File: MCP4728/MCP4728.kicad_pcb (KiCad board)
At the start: 2 copper layers, 25.4 x 17.8 mm, 22 parts, among them J1 Conn_01x06, J2 Conn_01x04, J3 Conn_01x06, J4 Conn_01x04, U1 MCP4728

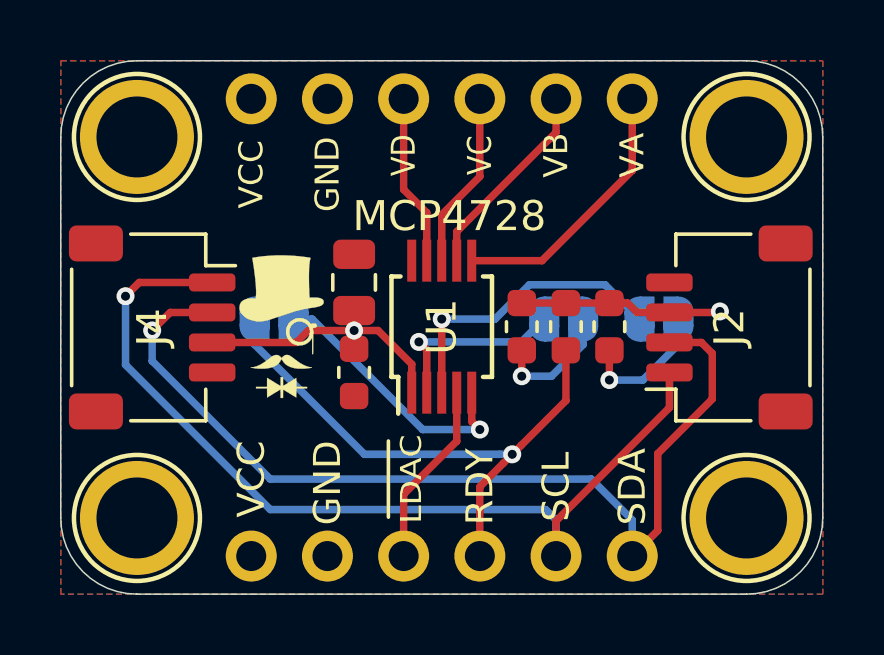
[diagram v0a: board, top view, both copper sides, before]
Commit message: Copper Pour Edits
Copper pour reduced to have 0.2mm edge clearance
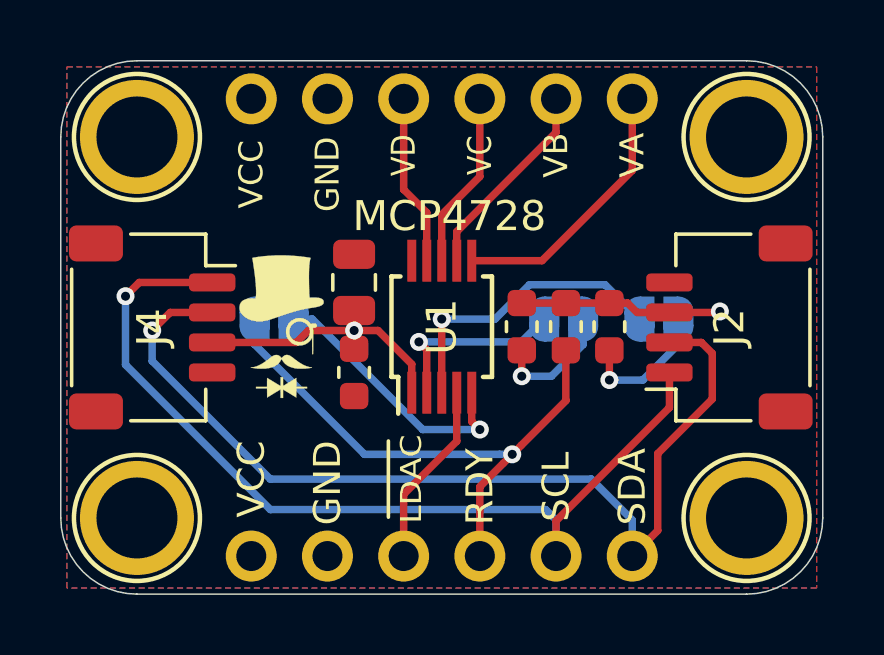
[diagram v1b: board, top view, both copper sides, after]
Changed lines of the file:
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@@
   )
   (setup
-    (last_trace_width 0.3)
+    (last_trace_width 0.127)
     (user_trace_width 0.2)
     (user_trace_width 0.25)
@@
     (polygon
       (pts
-        (xy 52.578 27.0764) (xy 77.978 27.0764) (xy 77.978 44.8564) (xy 52.578 44.8564)
+        (xy 52.7812 27.2796) (xy 77.7748 27.2796) (xy 77.7748 44.6532) (xy 52.7812 44.6532)
       )
     )
@@
     (polygon
       (pts
-        (xy 52.578 27.0764) (xy 77.978 27.0764) (xy 77.978 44.8564) (xy 52.578 44.8564)
+        (xy 52.7812 27.2796) (xy 77.7748 27.2796) (xy 77.7748 44.6532) (xy 52.7812 44.6532)
       )
     )

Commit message: Phew...
almost a screw up
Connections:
- SCL pad 1: SCL -> SCL_5V
- SDA pad 1: SDA -> SDA_5V
- U1 pad 2: SCL -> SCL_5V
- U1 pad 3: SDA -> SDA_5V
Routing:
- net SDA_5V: track 32.1 -> 51.4 mm, vias 1 -> 3
- net SCL_5V: track 30.7 -> 45.0 mm, vias 1 -> 3
- net SDA: track 9.99 -> 0.00 mm, vias 1 -> 0
- net SCL: track 6.29 -> 0.00 mm, vias 1 -> 0
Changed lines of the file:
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@@
     (thickness 1.6)
     (drawings 32)
-    (tracks 95)
+    (tracks 108)
     (zones 0)
     (modules 22)
-    (nets 16)
+    (nets 14)
   )
   (page User 132.004 102.006)
   (title_block
     (title "MCP4728 Breakout")
-    (date 2020-01-23)
-    (rev 2)
+    (date 2020-03-10)
+    (rev 3)
     (company SirBoard)
     (comment 1 "4 Channel I2C DAC with 12 Bit Resolution")
@@
     (34 B.Paste user hide)
     (35 F.Paste user hide)
-    (36 B.SilkS user hide)
+    (36 B.SilkS user)
     (37 F.SilkS user)
     (38 B.Mask user hide)
@@
   )
   (setup
-    (last_trace_width 0.127)
+    (last_trace_width 0.2)
     (user_trace_width 0.2)
     (user_trace_width 0.25)
@@
   (net 11 "Net-(JP1-Pad2)")
   (net 12 "Net-(JP2-Pad2)")
-  (net 13 SCL)
-  (net 14 "Net-(JP3-Pad2)")
-  (net 15 SDA)
+  (net 13 "Net-(JP3-Pad2)")
   (net_class Default "This is the default net class."
     (clearance 0.127)
@@
     (add_net "Net-(JP3-Pad2)")
     (add_net RDY)
-    (add_net SCL)
     (add_net SCL_5V)
-    (add_net SDA)
     (add_net SDA_5V)
     (add_net VCC)
@@
       (net 6 LDAC))
     (pad 3 smd rect (at -2.2 0 90) (size 1.4 0.3) (layers F.Cu F.Paste F.Mask)
-      (net 15 SDA))
+      (net 3 SDA_5V))
     (pad 2 smd rect (at -2.2 -0.5 90) (size 1.4 0.3) (layers F.Cu F.Paste F.Mask)
-      (net 13 SCL))
+      (net 2 SCL_5V))
     (pad 1 smd rect (at -2.2 -1 90) (size 1.4 0.3) (layers F.Cu F.Paste F.Mask)
       (net 4 VCC))
@@
     (fp_line (start -0.8 0.4) (end -0.8 -0.4) (layer F.Fab) (width 0.1))
     (pad 2 smd roundrect (at 0.7875 0 270) (size 0.875 0.95) (layers F.Cu F.Paste F.Mask) (roundrect_rratio 0.25)
-      (net 14 "Net-(JP3-Pad2)"))
+      (net 13 "Net-(JP3-Pad2)"))
     (pad 1 smd roundrect (at -0.7875 0 270) (size 0.875 0.95) (layers F.Cu F.Paste F.Mask) (roundrect_rratio 0.25)
       (net 4 VCC))
@@
     (fp_arc (start 0.7 0.3) (end 1.4 0.3) (angle 90) (layer B.SilkS) (width 0.12))
     (pad 2 smd custom (at 0.65 0) (size 1 0.5) (layers B.Cu B.Mask)
-      (net 14 "Net-(JP3-Pad2)") (zone_connect 2)
+      (net 13 "Net-(JP3-Pad2)") (zone_connect 2)
       (options (clearance outline) (anchor rect))
       (primitives
@@
       ))
     (pad 1 smd custom (at -0.65 0) (size 1 0.5) (layers B.Cu B.Mask)
-      (net 15 SDA) (zone_connect 2)
+      (net 3 SDA_5V) (zone_connect 2)
       (options (clearance outline) (anchor rect))
       (primitives
@@
       ))
     (pad 1 smd custom (at -0.65 0) (size 1 0.5) (layers B.Cu B.Mask)
-      (net 13 SCL) (zone_connect 2)
+      (net 2 SCL_5V) (zone_connect 2)
       (options (clearance outline) (anchor rect))
       (primitives
@@
   (segment (start 69.992 36.534592) (end 68.934592 37.592) (width 0.25) (layer B.Cu) (net 12))
   (segment (start 67.945 37.592) (end 67.945 36.7285) (width 0.25) (layer F.Cu) (net 12))
-  (segment (start 64.778 36.711) (end 64.516 36.449) (width 0.25) (layer F.Cu) (net 13))
-  (segment (start 64.778 38.141) (end 64.778 36.711) (width 0.25) (layer F.Cu) (net 13))
-  (via (at 64.516 36.449) (size 0.6) (drill 0.3) (layers F.Cu B.Cu) (net 13))
-  (segment (start 67.93 36.449) (end 64.516 36.449) (width 0.25) (layer B.Cu) (net 13))
-  (segment (start 68.692 35.687) (end 67.93 36.449) (width 0.25) (layer B.Cu) (net 13))
-  (via (at 70.866 37.719) (size 0.6) (drill 0.3) (layers F.Cu B.Cu) (net 14))
-  (segment (start 71.982592 37.719) (end 70.866 37.719) (width 0.25) (layer B.Cu) (net 14))
-  (segment (start 73.167 35.687) (end 73.167 36.534592) (width 0.25) (layer B.Cu) (net 14))
-  (segment (start 73.167 36.534592) (end 71.982592 37.719) (width 0.25) (layer B.Cu) (net 14))
-  (segment (start 70.866 37.719) (end 70.866 36.7285) (width 0.25) (layer F.Cu) (net 14))
-  (segment (start 71.867 35.687) (end 70.724 34.544) (width 0.25) (layer B.Cu) (net 15))
-  (segment (start 70.724 34.544) (end 68.199 34.544) (width 0.25) (layer B.Cu) (net 15))
-  (via (at 65.278 35.687) (size 0.6) (drill 0.3) (layers F.Cu B.Cu) (net 15))
-  (segment (start 68.199 34.544) (end 67.056 35.687) (width 0.25) (layer B.Cu) (net 15))
-  (segment (start 67.056 35.687) (end 65.278 35.687) (width 0.25) (layer B.Cu) (net 15))
-  (segment (start 65.278 35.687) (end 65.278 38.141) (width 0.25) (layer F.Cu) (net 15))
+  (segment (start 64.778 36.711) (end 64.516 36.449) (width 0.25) (layer F.Cu) (net 2))
+  (segment (start 64.778 38.141) (end 64.778 36.711) (width 0.25) (layer F.Cu) (net 2))
+  (via (at 64.516 36.449) (size 0.6) (drill 0.3) (layers F.Cu B.Cu) (net 2))
+  (segment (start 68.692 35.687) (end 67.93 36.449) (width 0.25) (layer B.Cu) (net 2))
+  (segment (start 72.8665 38.6395) (end 72.8665 38.6395) (width 0.25) (layer F.Cu) (net 2))
+  (via (at 72.8665 38.6395) (size 0.6) (drill 0.3) (layers F.Cu B.Cu) (net 2))
+  (segment (start 66.2432 36.449) (end 66.2432 37.2364) (width 0.2) (layer B.Cu) (net 2))
+  (segment (start 67.93 36.449) (end 66.2432 36.449) (width 0.25) (layer B.Cu) (net 2))
+  (segment (start 66.2432 36.449) (end 64.516 36.449) (width 0.25) (layer B.Cu) (net 2))
+  (segment (start 67.6463 38.6395) (end 72.8665 38.6395) (width 0.2) (layer B.Cu) (net 2))
+  (segment (start 66.2432 37.2364) (end 67.6463 38.6395) (width 0.2) (layer B.Cu) (net 2))
+  (via (at 70.866 37.719) (size 0.6) (drill 0.3) (layers F.Cu B.Cu) (net 13))
+  (segment (start 71.982592 37.719) (end 70.866 37.719) (width 0.25) (layer B.Cu) (net 13))
+  (segment (start 73.167 35.687) (end 73.167 36.534592) (width 0.25) (layer B.Cu) (net 13))
+  (segment (start 73.167 36.534592) (end 71.982592 37.719) (width 0.25) (layer B.Cu) (net 13))
+  (segment (start 70.866 37.719) (end 70.866 36.7285) (width 0.25) (layer F.Cu) (net 13))
+  (segment (start 71.867 35.687) (end 70.724 34.544) (width 0.25) (layer B.Cu) (net 3))
+  (segment (start 70.724 34.544) (end 68.199 34.544) (width 0.25) (layer B.Cu) (net 3))
+  (via (at 65.278 35.687) (size 0.6) (drill 0.3) (layers F.Cu B.Cu) (net 3))
+  (segment (start 68.199 34.544) (end 67.056 35.687) (width 0.25) (layer B.Cu) (net 3))
+  (segment (start 67.056 35.687) (end 65.278 35.687) (width 0.25) (layer B.Cu) (net 3))
+  (segment (start 65.278 35.687) (end 65.278 38.141) (width 0.25) (layer F.Cu) (net 3))
+  (segment (start 74.295 38.354) (end 74.295 38.354) (width 0.25) (layer F.Cu) (net 3))
+  (via (at 74.295 38.354) (size 0.6) (drill 0.3) (layers F.Cu B.Cu) (net 3))
+  (segment (start 70.724 34.544) (end 71.0796 34.1884) (width 0.2) (layer B.Cu) (net 3))
+  (segment (start 71.0796 34.1884) (end 74.9554 34.1884) (width 0.2) (layer B.Cu) (net 3))
+  (segment (start 74.9554 34.1884) (end 75.4888 34.7218) (width 0.2) (layer B.Cu) (net 3))
+  (segment (start 75.4888 37.1602) (end 74.295 38.354) (width 0.2) (layer B.Cu) (net 3))
+  (segment (start 75.4888 34.7218) (end 75.4888 37.1602) (width 0.2) (layer B.Cu) (net 3))
   (zone (net 4) (net_name VCC) (layer B.Cu) (hatch none 0.508)
     (connect_pads (clearance 0.15))

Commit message: Auto stash before revert of "Board Revision"
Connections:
- SCL pad 1: SCL_5V -> SCL
- SDA pad 1: SDA_5V -> SDA
- U1 pad 2: SCL_5V -> SCL
- U1 pad 3: SDA_5V -> SDA
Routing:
- net SDA_5V: track 51.4 -> 32.1 mm, vias 3 -> 1
- net SCL_5V: track 45.0 -> 30.7 mm, vias 3 -> 1
- net SDA: track 0.00 -> 9.99 mm, vias 0 -> 1
- net SCL: track 0.00 -> 6.29 mm, vias 0 -> 1
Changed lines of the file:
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@@
     (thickness 1.6)
     (drawings 32)
-    (tracks 108)
+    (tracks 95)
     (zones 0)
     (modules 22)
-    (nets 14)
+    (nets 16)
   )
   (page User 132.004 102.006)
   (title_block
     (title "MCP4728 Breakout")
-    (date 2020-03-10)
-    (rev 3)
+    (date 2020-01-23)
+    (rev 2)
     (company SirBoard)
     (comment 1 "4 Channel I2C DAC with 12 Bit Resolution")
@@
     (34 B.Paste user hide)
     (35 F.Paste user hide)
-    (36 B.SilkS user)
+    (36 B.SilkS user hide)
     (37 F.SilkS user)
     (38 B.Mask user hide)
@@
   )
   (setup
-    (last_trace_width 0.2)
+    (last_trace_width 0.127)
     (user_trace_width 0.2)
     (user_trace_width 0.25)
@@
   (net 11 "Net-(JP1-Pad2)")
   (net 12 "Net-(JP2-Pad2)")
-  (net 13 "Net-(JP3-Pad2)")
+  (net 13 SCL)
+  (net 14 "Net-(JP3-Pad2)")
+  (net 15 SDA)
   (net_class Default "This is the default net class."
     (clearance 0.127)
@@
     (add_net "Net-(JP3-Pad2)")
     (add_net RDY)
+    (add_net SCL)
     (add_net SCL_5V)
+    (add_net SDA)
     (add_net SDA_5V)
     (add_net VCC)
@@
       (net 6 LDAC))
     (pad 3 smd rect (at -2.2 0 90) (size 1.4 0.3) (layers F.Cu F.Paste F.Mask)
-      (net 3 SDA_5V))
+      (net 15 SDA))
     (pad 2 smd rect (at -2.2 -0.5 90) (size 1.4 0.3) (layers F.Cu F.Paste F.Mask)
-      (net 2 SCL_5V))
+      (net 13 SCL))
     (pad 1 smd rect (at -2.2 -1 90) (size 1.4 0.3) (layers F.Cu F.Paste F.Mask)
       (net 4 VCC))
@@
     (fp_line (start -0.8 0.4) (end -0.8 -0.4) (layer F.Fab) (width 0.1))
     (pad 2 smd roundrect (at 0.7875 0 270) (size 0.875 0.95) (layers F.Cu F.Paste F.Mask) (roundrect_rratio 0.25)
-      (net 13 "Net-(JP3-Pad2)"))
+      (net 14 "Net-(JP3-Pad2)"))
     (pad 1 smd roundrect (at -0.7875 0 270) (size 0.875 0.95) (layers F.Cu F.Paste F.Mask) (roundrect_rratio 0.25)
       (net 4 VCC))
@@
     (fp_arc (start 0.7 0.3) (end 1.4 0.3) (angle 90) (layer B.SilkS) (width 0.12))
     (pad 2 smd custom (at 0.65 0) (size 1 0.5) (layers B.Cu B.Mask)
-      (net 13 "Net-(JP3-Pad2)") (zone_connect 2)
+      (net 14 "Net-(JP3-Pad2)") (zone_connect 2)
       (options (clearance outline) (anchor rect))
       (primitives
@@
       ))
     (pad 1 smd custom (at -0.65 0) (size 1 0.5) (layers B.Cu B.Mask)
-      (net 3 SDA_5V) (zone_connect 2)
+      (net 15 SDA) (zone_connect 2)
       (options (clearance outline) (anchor rect))
       (primitives
@@
       ))
     (pad 1 smd custom (at -0.65 0) (size 1 0.5) (layers B.Cu B.Mask)
-      (net 2 SCL_5V) (zone_connect 2)
+      (net 13 SCL) (zone_connect 2)
       (options (clearance outline) (anchor rect))
       (primitives
@@
   (segment (start 69.992 36.534592) (end 68.934592 37.592) (width 0.25) (layer B.Cu) (net 12))
   (segment (start 67.945 37.592) (end 67.945 36.7285) (width 0.25) (layer F.Cu) (net 12))
-  (segment (start 64.778 36.711) (end 64.516 36.449) (width 0.25) (layer F.Cu) (net 2))
-  (segment (start 64.778 38.141) (end 64.778 36.711) (width 0.25) (layer F.Cu) (net 2))
-  (via (at 64.516 36.449) (size 0.6) (drill 0.3) (layers F.Cu B.Cu) (net 2))
-  (segment (start 68.692 35.687) (end 67.93 36.449) (width 0.25) (layer B.Cu) (net 2))
-  (segment (start 72.8665 38.6395) (end 72.8665 38.6395) (width 0.25) (layer F.Cu) (net 2))
-  (via (at 72.8665 38.6395) (size 0.6) (drill 0.3) (layers F.Cu B.Cu) (net 2))
-  (segment (start 66.2432 36.449) (end 66.2432 37.2364) (width 0.2) (layer B.Cu) (net 2))
-  (segment (start 67.93 36.449) (end 66.2432 36.449) (width 0.25) (layer B.Cu) (net 2))
-  (segment (start 66.2432 36.449) (end 64.516 36.449) (width 0.25) (layer B.Cu) (net 2))
-  (segment (start 67.6463 38.6395) (end 72.8665 38.6395) (width 0.2) (layer B.Cu) (net 2))
-  (segment (start 66.2432 37.2364) (end 67.6463 38.6395) (width 0.2) (layer B.Cu) (net 2))
-  (via (at 70.866 37.719) (size 0.6) (drill 0.3) (layers F.Cu B.Cu) (net 13))
-  (segment (start 71.982592 37.719) (end 70.866 37.719) (width 0.25) (layer B.Cu) (net 13))
-  (segment (start 73.167 35.687) (end 73.167 36.534592) (width 0.25) (layer B.Cu) (net 13))
-  (segment (start 73.167 36.534592) (end 71.982592 37.719) (width 0.25) (layer B.Cu) (net 13))
-  (segment (start 70.866 37.719) (end 70.866 36.7285) (width 0.25) (layer F.Cu) (net 13))
-  (segment (start 71.867 35.687) (end 70.724 34.544) (width 0.25) (layer B.Cu) (net 3))
-  (segment (start 70.724 34.544) (end 68.199 34.544) (width 0.25) (layer B.Cu) (net 3))
-  (via (at 65.278 35.687) (size 0.6) (drill 0.3) (layers F.Cu B.Cu) (net 3))
-  (segment (start 68.199 34.544) (end 67.056 35.687) (width 0.25) (layer B.Cu) (net 3))
-  (segment (start 67.056 35.687) (end 65.278 35.687) (width 0.25) (layer B.Cu) (net 3))
-  (segment (start 65.278 35.687) (end 65.278 38.141) (width 0.25) (layer F.Cu) (net 3))
-  (segment (start 74.295 38.354) (end 74.295 38.354) (width 0.25) (layer F.Cu) (net 3))
-  (via (at 74.295 38.354) (size 0.6) (drill 0.3) (layers F.Cu B.Cu) (net 3))
-  (segment (start 70.724 34.544) (end 71.0796 34.1884) (width 0.2) (layer B.Cu) (net 3))
-  (segment (start 71.0796 34.1884) (end 74.9554 34.1884) (width 0.2) (layer B.Cu) (net 3))
-  (segment (start 74.9554 34.1884) (end 75.4888 34.7218) (width 0.2) (layer B.Cu) (net 3))
-  (segment (start 75.4888 37.1602) (end 74.295 38.354) (width 0.2) (layer B.Cu) (net 3))
-  (segment (start 75.4888 34.7218) (end 75.4888 37.1602) (width 0.2) (layer B.Cu) (net 3))
+  (segment (start 64.778 36.711) (end 64.516 36.449) (width 0.25) (layer F.Cu) (net 13))
+  (segment (start 64.778 38.141) (end 64.778 36.711) (width 0.25) (layer F.Cu) (net 13))
+  (via (at 64.516 36.449) (size 0.6) (drill 0.3) (layers F.Cu B.Cu) (net 13))
+  (segment (start 67.93 36.449) (end 64.516 36.449) (width 0.25) (layer B.Cu) (net 13))
+  (segment (start 68.692 35.687) (end 67.93 36.449) (width 0.25) (layer B.Cu) (net 13))
+  (via (at 70.866 37.719) (size 0.6) (drill 0.3) (layers F.Cu B.Cu) (net 14))
+  (segment (start 71.982592 37.719) (end 70.866 37.719) (width 0.25) (layer B.Cu) (net 14))
+  (segment (start 73.167 35.687) (end 73.167 36.534592) (width 0.25) (layer B.Cu) (net 14))
+  (segment (start 73.167 36.534592) (end 71.982592 37.719) (width 0.25) (layer B.Cu) (net 14))
+  (segment (start 70.866 37.719) (end 70.866 36.7285) (width 0.25) (layer F.Cu) (net 14))
+  (segment (start 71.867 35.687) (end 70.724 34.544) (width 0.25) (layer B.Cu) (net 15))
+  (segment (start 70.724 34.544) (end 68.199 34.544) (width 0.25) (layer B.Cu) (net 15))
+  (via (at 65.278 35.687) (size 0.6) (drill 0.3) (layers F.Cu B.Cu) (net 15))
+  (segment (start 68.199 34.544) (end 67.056 35.687) (width 0.25) (layer B.Cu) (net 15))
+  (segment (start 67.056 35.687) (end 65.278 35.687) (width 0.25) (layer B.Cu) (net 15))
+  (segment (start 65.278 35.687) (end 65.278 38.141) (width 0.25) (layer F.Cu) (net 15))
   (zone (net 4) (net_name VCC) (layer B.Cu) (hatch none 0.508)
     (connect_pads (clearance 0.15))
